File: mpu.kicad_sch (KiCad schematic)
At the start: 166 parts, among them J1 USB_OTG, J2 DIN41612_02x10_AB, J3 USB_OTG, J4 Conn_02x20_Counter_Clockwise, J5 Conn_01x15_Socket, U3 ECMF02-2AMX6, U4 ECMF02-2AMX6, U5 STM32MP157FADx, X1 ASE-24MHz

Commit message: DDR added switch backs
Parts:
- C32, C33, C34, C35, C36: footprint Capacitor_SMD:C_0402_1005Metric -> Capacitor_SMD:C_0201_0603Metric
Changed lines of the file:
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@@
 			)
 		)
-		(property "Footprint" "Capacitor_SMD:C_0402_1005Metric"
+		(property "Footprint" "Capacitor_SMD:C_0201_0603Metric"
 			(at 411.1752 276.86 0)
 			(effects
@@
 			)
 		)
-		(property "Footprint" "Capacitor_SMD:C_0402_1005Metric"
+		(property "Footprint" "Capacitor_SMD:C_0201_0603Metric"
 			(at 461.9752 276.86 0)
 			(effects
@@
 			)
 		)
-		(property "Footprint" "Capacitor_SMD:C_0402_1005Metric"
+		(property "Footprint" "Capacitor_SMD:C_0201_0603Metric"
 			(at 449.2752 276.86 0)
 			(effects
@@
 			)
 		)
-		(property "Footprint" "Capacitor_SMD:C_0402_1005Metric"
+		(property "Footprint" "Capacitor_SMD:C_0201_0603Metric"
 			(at 423.8752 276.86 0)
 			(effects
@@
 			)
 		)
-		(property "Footprint" "Capacitor_SMD:C_0402_1005Metric"
+		(property "Footprint" "Capacitor_SMD:C_0201_0603Metric"
 			(at 436.5752 276.86 0)
 			(effects

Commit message: More DDR Routing
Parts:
- R51: footprint Resistor_SMD:R_0402_1005Metric -> Resistor_SMD:R_0201_0603Metric
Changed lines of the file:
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@@
 			)
 		)
-		(property "Footprint" "Resistor_SMD:R_0402_1005Metric"
+		(property "Footprint" "Resistor_SMD:R_0201_0603Metric"
 			(at 465.582 316.23 0)
 			(effects

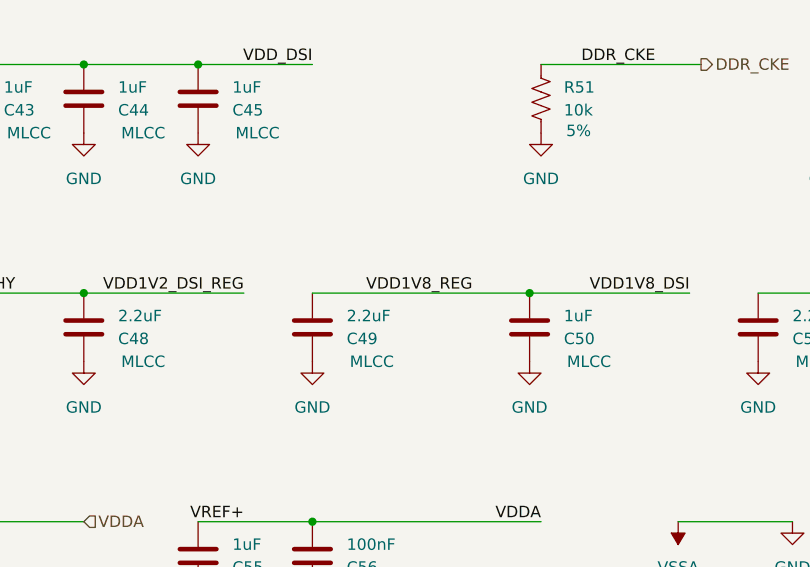
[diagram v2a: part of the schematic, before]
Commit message: More DDR Routing
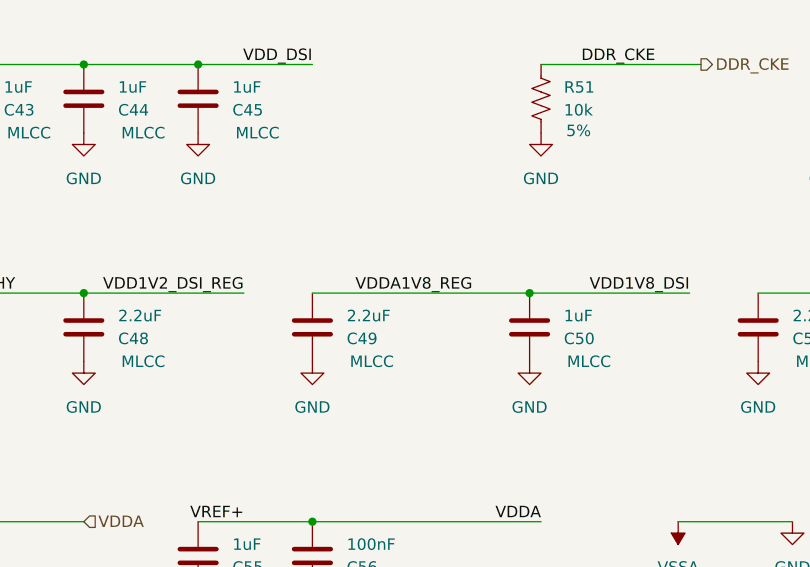
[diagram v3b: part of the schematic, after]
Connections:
- net VDDA1V8_REG is gone; now on net VDD1V8_DSI: U5.1H5 (VDDA1V8_REG)
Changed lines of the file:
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@@
 		)
 	)
-	(label "VDD1V8_REG"
+	(label "VDDA1V8_REG"
 		(at 453.39 337.82 180)
 		(fields_autoplaced yes)

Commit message: Added in new MPU
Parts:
- added R148: 3k, Resistor_SMD:R_0201_0603Metric, symbol SparkFun-Resistor:R
- added R149, R150: 0, Resistor_SMD:R_0402_1005Metric, symbol SparkFun-Resistor:R
- added U9: STM32MP153AABx, Package_BGA:ST_LFBGA-354_16x16mm_Layout19x19_P0.8mm, symbol MCU_ST_STM32MP1:STM32MP153AABx
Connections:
- net A0: now also U9.H18 (DDR_A0)
- net A1: now also U9.M17 (DDR_A1)
- net A10: now also U9.M19 (DDR_A10)
- net A11: now also U9.M18 (DDR_A11)
- net A12: now also U9.L17 (DDR_A12)
- net A13: now also U9.F17 (DDR_A13)
- net A14: now also U9.N18 (DDR_A14)
- net A15: now also U9.L16 (DDR_A15)
- net A2: now also U9.G18 (DDR_A2)
- net A3: now also U9.F19 (DDR_A3)
- net A4: now also U9.P17 (DDR_A4)
- net A5: now also U9.H17 (DDR_A5)
- net A6: now also U9.N16 (DDR_A6)
- net A7: now also U9.E17 (DDR_A7)
- net A8: now also U9.R17 (DDR_A8)
- net A9: now also U9.G17 (DDR_A9)
- net BOOT0: now also U9.K1 (BOOT0)
- net BOOT1: now also U9.K4 (BOOT1)
- net BOOT2: now also U9.L2 (BOOT2)
- net DDR_BA0: now also U9.G19 (DDR_BA0)
- net DDR_BA1: now also U9.N17 (DDR_BA1)
- net DDR_BA2: now also U9.J16 (DDR_BA2)
- net DDR_CAS: now also U9.K17 (DDR_CASN)
- net DDR_CKE: now also U9.P19 (DDR_CKE)
- net DDR_CLK_N: now also U9.K19 (DDR_CLKN)
- net DDR_CLK_P: now also U9.L19 (DDR_CLKP)
- net DDR_CS: now also U9.J18 (DDR_CSN)
- net DDR_DQML: now also U9.C18 (DDR_DQM0)
- net DDR_DQMU: now also U9.U18 (DDR_DQM1)
- net DDR_DQS0_N: now also U9.B19 (DDR_DQS0N)
- net DDR_DQS0_P: now also U9.C19 (DDR_DQS0P)
- net DDR_DQS1_N: now also U9.T19 (DDR_DQS1N)
- net DDR_DQS1_P: now also U9.U19 (DDR_DQS1P)
- net DDR_ODT: now also U9.H19 (DDR_ODT)
- net DDR_RAS: now also U9.L18 (DDR_RASN)
- net DDR_RESET: now also U9.G16 (DDR_RESETN)
- net DDR_WE: now also U9.J17 (DDR_WEN)
- net DQ0: now also U9.A17 (DDR_DQ0)
- net DQ1: now also U9.A18 (DDR_DQ1)
- net DQ10: now also U9.R18 (DDR_DQ10)
- net DQ11: now also U9.V19 (DDR_DQ11)
- net DQ12: now also U9.W18 (DDR_DQ12)
- net DQ13: now also U9.T18 (DDR_DQ13)
- net DQ14: now also U9.V18 (DDR_DQ14)
- net DQ15: now also U9.W17 (DDR_DQ15)
- net DQ2: now also U9.D18 (DDR_DQ2)
- net DQ3: now also U9.B17 (DDR_DQ3)
- net DQ4: now also U9.E18 (DDR_DQ4)
- net DQ5: now also U9.D17 (DDR_DQ5)
- net DQ6: now also U9.D19 (DDR_DQ6)
- net DQ7: now also U9.B18 (DDR_DQ7)
- net DQ8: now also U9.P18 (DDR_DQ8)
- net DQ9: now also U9.T17 (DDR_DQ9)
- net GND: now also R148.2, R149.2, R150.2, U9.T15 (BYPASS_REG1V8)
- net JTCK: now also U9.D16 (JTCK)
- net JTDI: now also U9.D13 (JTDI)
- net JTDO: now also U9.D14 (JTDO)
- net JTMS: now also U9.D15 (JTMS)
- net OSC_IN: now also U9.M1 (PH0)
- net OSC_OUT: now also U9.M2 (PH1)
- net PWR_LP: now also U9.P1 (PWR_LP)
- net PWR_ON: now also U9.L1 (PWR_ON)
- net USB_D1_N: now also U9.W14 (USB_DM1)
- net USB_D1_P: now also U9.V14 (USB_DP1)
- net USB_D2_N: now also U9.V13 (USB_DM2)
- net USB_D2_P: now also U9.W13 (USB_DP2)
- net USB_RREF: now also R148.1, U9.V16 (USB_RREF)
- net VBUS_OTG: now also U9.U15 (OTG_VBUS)
- net VDD: now also U9.H3 (VBAT), U9.K6 (VDD), U9.L5 (VDD), U9.L7 (VDD), U9.M6 (VDD), U9.M8 (VDD), U9.N1 (PDR_ON_CORE), U9.N2 (PDR_ON), U9.N5 (VDD), U9.N7 (VDD), U9.N9 (VDD), U9.P10 (VDD), U9.P6 (VDD), U9.P8 (VDD), U9.R11 (VDD), U9.R7 (VDD), U9.R9 (VDD)
- net VDD1V1_REG: now also U9.W11 (VDDA1V1_REG)
- net VDD1V8_DSI: now also U9.V11 (VDDA1V8_REG)
- net VDDA: now also U9.M4 (VDDA), U9.N3 (VREF+)
- net VDD_CORE: now also U9.E11 (VDDCORE), U9.E13 (VDDCORE), U9.E7 (VDDCORE), U9.E9 (VDDCORE), U9.F10 (VDDCORE), U9.F12 (VDDCORE), U9.F4 (VDDCORE), U9.F6 (VDDCORE), U9.F8 (VDDCORE), U9.G11 (VDDCORE), U9.G5 (VDDCORE), U9.G7 (VDDCORE), U9.G9 (VDDCORE), U9.H10 (VDDCORE), U9.H12 (VDDCORE), U9.H4 (VDDCORE), U9.H6 (VDDCORE), U9.H8 (VDDCORE), U9.J11 (VDDCORE), U9.J13 (VDDCORE), U9.J7 (VDDCORE), U9.J9 (VDDCORE), U9.K10 (VDDCORE), U9.K12 (VDDCORE), U9.K8 (VDDCORE), U9.L11 (VDDCORE), U9.L13 (VDDCORE), U9.L9 (VDDCORE), U9.M10 (VDDCORE), U9.M12 (VDDCORE), U9.N11 (VDDCORE), U9.N13 (VDDCORE), U9.P12 (VDDCORE), U9.R13 (VDDCORE)
- net VDD_DDR: now also U9.E15 (VDDQ_DDR), U9.F14 (VDDQ_DDR), U9.G15 (VDDQ_DDR), U9.H14 (VDDQ_DDR), U9.J15 (VDDQ_DDR), U9.K14 (VDDQ_DDR), U9.L15 (VDDQ_DDR), U9.M14 (VDDQ_DDR), U9.N15 (VDDQ_DDR), U9.P14 (VDDQ_DDR), U9.R15 (VDDQ_DDR)
- net VREF_DDR: now also U9.W16 (DDR_VREF)
- net ZQ: now also U9.F18 (DDR_ZQ)
- net nRST: now also U9.J1 (NRST)
- net nRST_CORE: now also U9.J2 (NRST_CORE)
- net nTRST: now also U9.D12 (NJTRST)
- new net: R150.1, U9.K18 (DDR_DTO0)
- new net: U9.A1 (VSS), U9.A19 (VSS), U9.B2 (VSS), U9.B6 (VSS), U9.C12 (VSS), U9.C13 (VSS), U9.C14 (VSS), U9.C15 (VSS), U9.C16 (VSS), U9.C17 (VSS), U9.C3 (VSS), U9.D1 (VSS), U9.D4 (VSS), U9.D5 (VSS), U9.D8 (VSS), U9.E10 (VSS), U9.E12 (VSS), U9.E14 (VSS), U9.E16 (VSS), U9.E2 (VSS), U9.E4 (VSS), U9.E5 (VSS), U9.E6 (VSS), U9.E8 (VSS), U9.F11 (VSS), U9.F15 (VSS), U9.F5 (VSS), U9.F7 (VSS), U9.F9 (VSS), U9.G10 (VSS), U9.G12 (VSS), U9.G14 (VSS), U9.G2 (VSS), U9.G4 (VSS), U9.G6 (VSS), U9.G8 (VSS), U9.H11 (VSS), U9.H13 (VSS), U9.H15 (VSS), U9.H5 (VSS), U9.H7 (VSS), U9.H9 (VSS), U9.J10 (VSS), U9.J12 (VSS), U9.J14 (VSS), U9.J3 (VSS), U9.J6 (VSS), U9.J8 (VSS), U9.K11 (VSS), U9.K13 (VSS), U9.K15 (VSS), U9.K2 (VSS), U9.K5 (VSS), U9.K7 (VSS), U9.K9 (VSS), U9.L10 (VSS), U9.L12 (VSS), U9.L14 (VSS), U9.L6 (VSS), U9.L8 (VSS), U9.M11 (VSS), U9.M13 (VSS), U9.M15 (VSS), U9.M5 (VSS), U9.M7 (VSS), U9.M9 (VSS), U9.N10 (VSS), U9.N12 (VSS), U9.N14 (VSS), U9.N6 (VSS), U9.N8 (VSS), U9.P11 (VSS), U9.P13 (VSS), U9.P15 (VSS), U9.P7 (VSS), U9.P9 (VSS), U9.R10 (VSS), U9.R12 (VSS), U9.R14 (VSS), U9.R16 (VSS), U9.R2 (VSS), U9.R6 (VSS), U9.R8 (VSS), U9.T4 (VSS), U9.U17 (VSS), U9.U3 (VSS), U9.U6 (VSS), U9.U8 (VSS), U9.W1 (VSS), U9.W19 (VSS)
- new net: R149.1, U9.J19 (DDR_DTO1)
- new net: U9.N4 (VSSA), U9.P5 (VSSA), U9.R5 (VSSA)
- new net: U9.U13 (VSS_USBHS), U9.U14 (VSS_USBHS), U9.V12 (VSS_USBHS), U9.V15 (VSS_USBHS)
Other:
- moved on the sheet: C10, C11, C12, C13, C14, C15, C16, C17, C18, C19, C20, C21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

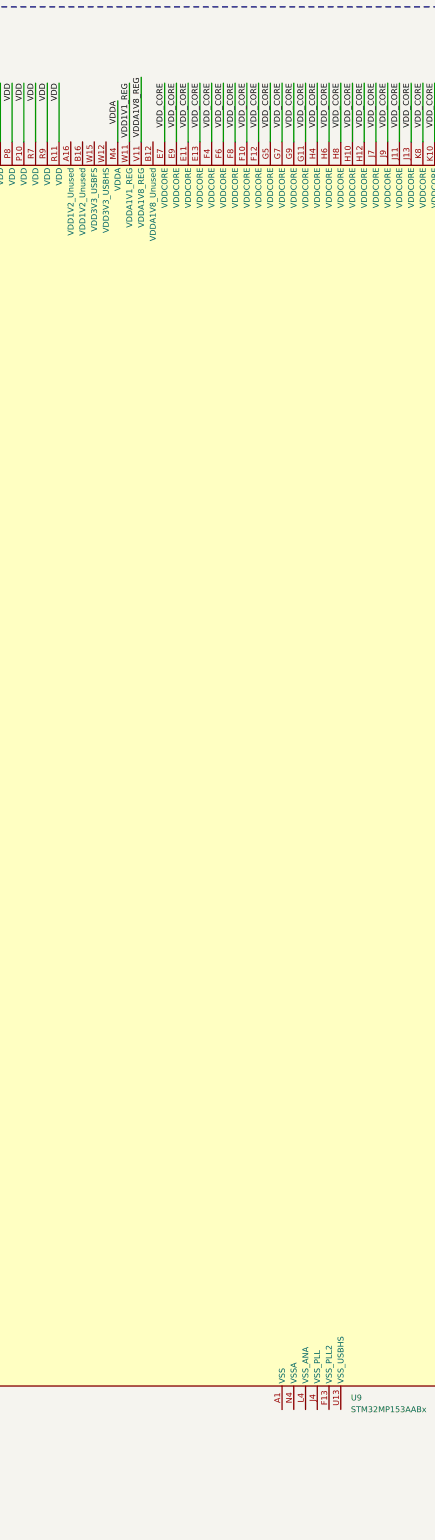
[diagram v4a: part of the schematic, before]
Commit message: Schemtic work to add in new MPU
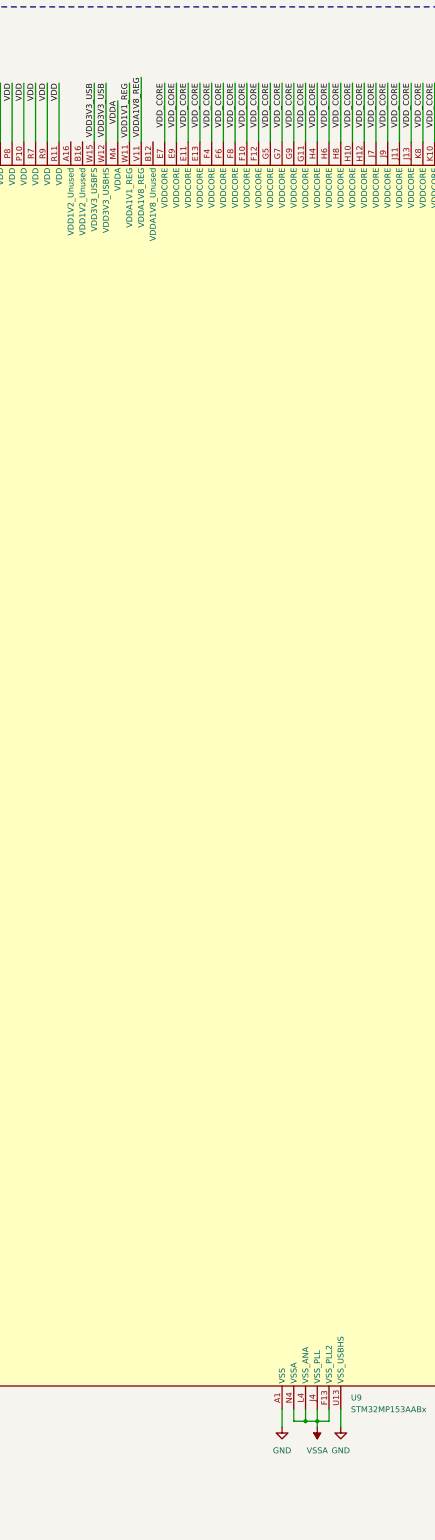
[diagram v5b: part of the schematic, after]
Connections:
- net GND: now also U9.A1 (VSS), U9.A19 (VSS), U9.B2 (VSS), U9.B6 (VSS), U9.C12 (VSS), U9.C13 (VSS), U9.C14 (VSS), U9.C15 (VSS), U9.C16 (VSS), U9.C17 (VSS), U9.C3 (VSS), U9.D1 (VSS), U9.D4 (VSS), U9.D5 (VSS), U9.D8 (VSS), U9.E10 (VSS), U9.E12 (VSS), U9.E14 (VSS), U9.E16 (VSS), U9.E2 (VSS), U9.E4 (VSS), U9.E5 (VSS), U9.E6 (VSS), U9.E8 (VSS), U9.F11 (VSS), U9.F13 (VSS_PLL2), U9.F15 (VSS), U9.F5 (VSS), U9.F7 (VSS), U9.F9 (VSS), U9.G10 (VSS), U9.G12 (VSS), U9.G14 (VSS), U9.G2 (VSS), U9.G4 (VSS), U9.G6 (VSS), U9.G8 (VSS), U9.H11 (VSS), U9.H13 (VSS), U9.H15 (VSS), U9.H5 (VSS), U9.H7 (VSS), U9.H9 (VSS), U9.J10 (VSS), U9.J12 (VSS), U9.J14 (VSS), U9.J3 (VSS), U9.J4 (VSS_PLL), U9.J6 (VSS), U9.J8 (VSS), U9.K11 (VSS), U9.K13 (VSS), U9.K15 (VSS), U9.K2 (VSS), U9.K5 (VSS), U9.K7 (VSS), U9.K9 (VSS), U9.L10 (VSS), U9.L12 (VSS), U9.L14 (VSS), U9.L4 (VSS_ANA), U9.L6 (VSS), U9.L8 (VSS), U9.M11 (VSS), U9.M13 (VSS), U9.M15 (VSS), U9.M5 (VSS), U9.M7 (VSS), U9.M9 (VSS), U9.N10 (VSS), U9.N12 (VSS), U9.N14 (VSS), U9.N4 (VSSA), U9.N6 (VSS), U9.N8 (VSS), U9.P11 (VSS), U9.P13 (VSS), U9.P15 (VSS), U9.P5 (VSSA), U9.P7 (VSS), U9.P9 (VSS), U9.R10 (VSS), U9.R12 (VSS), U9.R14 (VSS), U9.R16 (VSS), U9.R2 (VSS), U9.R5 (VSSA), U9.R6 (VSS), U9.R8 (VSS), U9.T4 (VSS), U9.U13 (VSS_USBHS), U9.U14 (VSS_USBHS), U9.U17 (VSS), U9.U3 (VSS), U9.U6 (VSS), U9.U8 (VSS), U9.V12 (VSS_USBHS), U9.V15 (VSS_USBHS), U9.W1 (VSS), U9.W19 (VSS)
- net VDD3V3_USB: now also U9.W12 (VDD3V3_USBHS), U9.W15 (VDD3V3_USBFS)

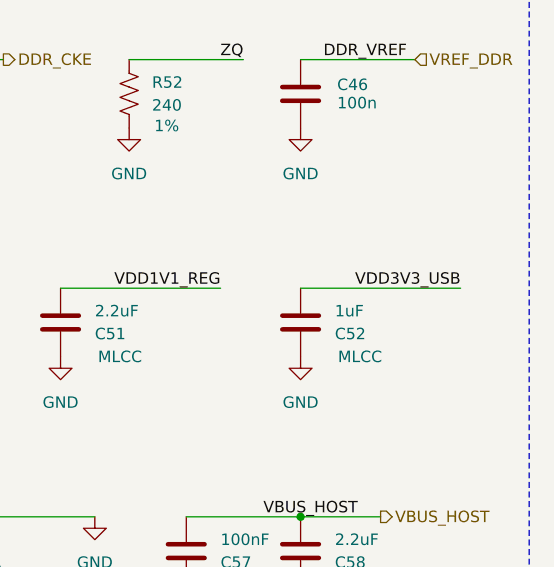
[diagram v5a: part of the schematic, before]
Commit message: Updating VDD_USB
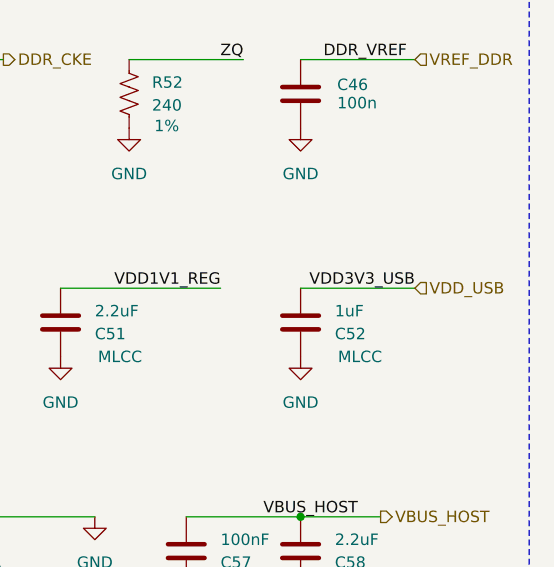
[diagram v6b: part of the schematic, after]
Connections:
- net VDD3V3_USB renamed VDD_USB
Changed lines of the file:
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@@
 	(wire
 		(pts
-			(xy 806.45 453.39) (xy 824.23 453.39)
+			(xy 806.45 453.39) (xy 819.15 453.39)
 		)
 		(stroke
@@
 	)
 	(label "VDD3V3_USB"
-		(at 824.23 453.39 180)
+		(at 819.15 453.39 180)
 		(fields_autoplaced yes)
 		(effects
@@
 		(fields_autoplaced yes)
 		(effects
+			(font
+				(size 1.27 1.27)
+			)
+			(justify left)
+		)
+	)
+	(hierarchical_label "VDD_USB"
+		(shape input)
+		(at 819.15 453.39 0)
+		(fields_autoplaced yes)
+		(effects

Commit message: Updating schematic
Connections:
- net nRST is gone; now on net SDMMC2_RESET: C10.1, C9.1, CR4.3 (I/O), J2.a8 (Pin_a8), SW1.2, U5.E2 (NRST), U9.J1 (NRST)
- net DBGACK: now also U9.P2 (PA13)
- net DBGRQ: now also U9.R1 (PA14)
- net ETH1_MDC_R: now also U9.V2 (PC1)
- net ETH1_RMII_CRS_DV: now also U9.T6 (PA7)
- net ETH1_RMII_REF_CLK: now also U9.U4 (PA1)
- net ETH1_RMII_RXD0: now also U9.V4 (PC5)
- net ETH1_RMII_RXD1: now also U9.W4 (PC4)
- net ETH1_RMII_TXD0_R: now also U9.T9 (PB13)
- net ETH1_RMII_TXD1_R: now also U9.V5 (PB12)
- net ETH1_RMII_TX_EN_R: now also U9.V1 (PB11)
- net ETH_CLK_R: now also U9.U7 (PG8)
- net ETH_MDIO: now also U9.W2 (PA2)
- net ETH_PHY_INTn: now also U9.F1 (PG12)
- net GND: now also U9.M3 (VREF-)
- net I2C_SCL: now also U9.V17 (PA11)
- net I2C_SDA: now also U9.U16 (PA12)
- net SDMMC2_CLK: now also U9.A5 (PE3)
- net SDMMC2_CMD: now also U9.A6 (PG6)
- net SDMMC2_D0: now also U9.C9 (PB14)
- net SDMMC2_D1: now also U9.A8 (PB15)
- net SDMMC2_D2: now also U9.A7 (PB3)
- net SDMMC2_D3: now also U9.B9 (PB4)
- net SDMMC2_D4: now also U9.B8 (PA8)
- net SDMMC2_D5: now also U9.C8 (PA9)
- net SDMMC2_D6: now also U9.B7 (PE5)
- net SDMMC2_D7: now also U9.C6 (PD3)
- net SDMMC2_STROBE: now also U9.B11 (PE4)
- net UART4_CTS: now also U9.W3 (PB0)
- net UART4_RTS: now also U9.C7 (PA15)
- net UART4_RX: now also U9.W6 (PB8)
- net UART4_TX: now also U9.T13 (PB2)
- net USB_OTG_ID: now also U9.T16 (PA10)
- net VDD: now also U9.G13 (VDD_PLL2), U9.J5 (VDD_PLL), U9.L3 (VDD_ANA)
- no-connect marks 2 -> 5

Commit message: Updated memory added 33ohm resistors
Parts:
- removed CR6, CR7: ESDA7P60-1U1M, footprints:ZDO_1610_STM, symbol ESDA7P60_1U1M:ESDA7P60-1U1M
- removed D17, D18: ECMF04-4HSWM10, footprints:QFN-10L_DTS, symbol ECMF04_4HSWM10:ECMF04-4HSWM10
- removed J2: DIN41612_02x10_AB, Connector_DIN:DIN41612_Q3_2x10_Male_Vertical_THT, symbol Connector:DIN41612_02x10_AB
- removed J5: Conn_01x15_Socket, Connector_FFC-FPC:Molex_200528-0150_1x15-1MP_P1.00mm_Horizontal, symbol Connector:Conn_01x15_Socket
- removed R100, R101, R102, R103, R104, R105, R106, R107, R108, R109, R110, R111, R112, R113, R114, R115, R116, R53, R54, R55, R56, R57, R58, R59, R60, R61, R62, R63, R64, R65, R66, R67, R68, R69, R70, R71, R72, R73, R74, R75, R76, R77, R78, R79, R80, R81, R82, R83, R84, R85, R86, R87, R88, R89, R90, R91, R92, R93, R94, R95, R96, R97, R98, R99: 10k, Resistor_SMD:R_0402_1005Metric, symbol SparkFun-Resistor:R
- removed R41: 3k, Resistor_SMD:R_0201_0603Metric, symbol SparkFun-Resistor:R
- removed R45, R47: 0, Resistor_SMD:R_0402_1005Metric, symbol SparkFun-Resistor:R
- removed U5: STM32MP157FADx, Package_BGA:ST_TFBGA-257_10x10mm_Layout19x19_P0.5mmP0.65mm, symbol MCU_ST_STM32MP1:STM32MP157FADx
- added J2: Conn_ARM_JTAG_SWD_20, Connector_PinHeader_1.27mm:PinHeader_2x10_P1.27mm_Vertical, symbol Connector:Conn_ARM_JTAG_SWD_20
- J4: footprint Connector_PinHeader_2.54mm:PinHeader_2x20_P2.54mm_Vertical -> Connector_PinHeader_1.27mm:PinHeader_2x20_P1.27mm_Vertical
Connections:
- net DBGACK: now also J2.19 (DBGACK/NC)
- net DBGRQ: now also J2.17 (DBGRQ/NC)
- net GND: now also J2.10 (GND), J2.12 (GND), J2.14 (GND), J2.16 (GND), J2.18 (GND), J2.20 (GND), J2.4 (GND), J2.6 (GND), J2.8 (GND); no longer J4.11 (Pin_11), J4.12 (Pin_12), J4.20 (Pin_20), J4.21 (Pin_21), J4.30 (Pin_30), J4.39 (Pin_39)
- net JTCK: now also J2.9 (TCK/SWCLK)
- net JTDI: now also J2.5 (TDI)
- net JTDO: now also J2.13 (TDO/SWO)
- net JTMS: now also J2.7 (TMS/SWDIO)
- net SDMMC2_RESET: now also J2.15 (~{SRST})
- net UART4_CTS: no longer J4.2 (Pin_2)
- net UART4_RTS: no longer J4.10 (Pin_10)
- net UART4_RX: no longer J4.6 (Pin_6)
- net UART4_TX: no longer J4.4 (Pin_4)
- net VDD: now also J2.1 (VTREF), J2.2 (VCC/NC); no longer J4.1 (Pin_1), J4.40 (Pin_40), J4.8 (Pin_8)
- net nTRST: now also J2.3 (~{TRST})
- net at R42.2: now also J2.11 (RTCK)
- net PA5: no longer names the net of J4.3 (Pin_3)
- net PA8: no longer names the net of J4.5 (Pin_5)
- net PB1: no longer names the net of J4.7 (Pin_7)
- net PB6: no longer names the net of J4.9 (Pin_9)
- net PC0: no longer names the net of J4.13 (Pin_13)
- net PC12: no longer names the net of J4.22 (Pin_22)
- net PC13: no longer names the net of J4.23 (Pin_23)
- net PC14: no longer names the net of J4.24 (Pin_24)
- net PC15: no longer names the net of J4.25 (Pin_25)
- net PC2: no longer names the net of J4.14 (Pin_14)
- net PC3: no longer names the net of J4.15 (Pin_15)
- net PC6: no longer names the net of J4.16 (Pin_16)
- net PC7: no longer names the net of J4.17 (Pin_17)
- net PC8: no longer names the net of J4.18 (Pin_18)
- net PC9: no longer names the net of J4.19 (Pin_19)
- net PD0: no longer names the net of J4.26 (Pin_26)
- net PD1: no longer names the net of J4.27 (Pin_27)
- net PD10: no longer names the net of J4.35 (Pin_35)
- net PD11: no longer names the net of J4.36 (Pin_36)
- net PD14: no longer names the net of J4.37 (Pin_37)
- net PD15: no longer names the net of J4.38 (Pin_38)
- net PD2: no longer names the net of J4.28 (Pin_28)
- net PD4: no longer names the net of J4.29 (Pin_29)
- net PD6: no longer names the net of J4.31 (Pin_31)
- net PD7: no longer names the net of J4.32 (Pin_32)
- net PD8: no longer names the net of J4.33 (Pin_33)
- net PD9: no longer names the net of J4.34 (Pin_34)
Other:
- note removed: "DSI"
- moved on the sheet: R148, R149, R150, R42, U9
